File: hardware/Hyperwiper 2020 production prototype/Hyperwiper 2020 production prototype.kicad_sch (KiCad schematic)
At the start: 29 parts, among them J1 Conn_01x05, K1 Main Power relay, K2 Wiper control relay, Q1 PN2222A, Q2 IRF540N, SW1 ON-OFF, SW2 SW_Reed, U1 Teensy4.0, U3 Voltage regulator

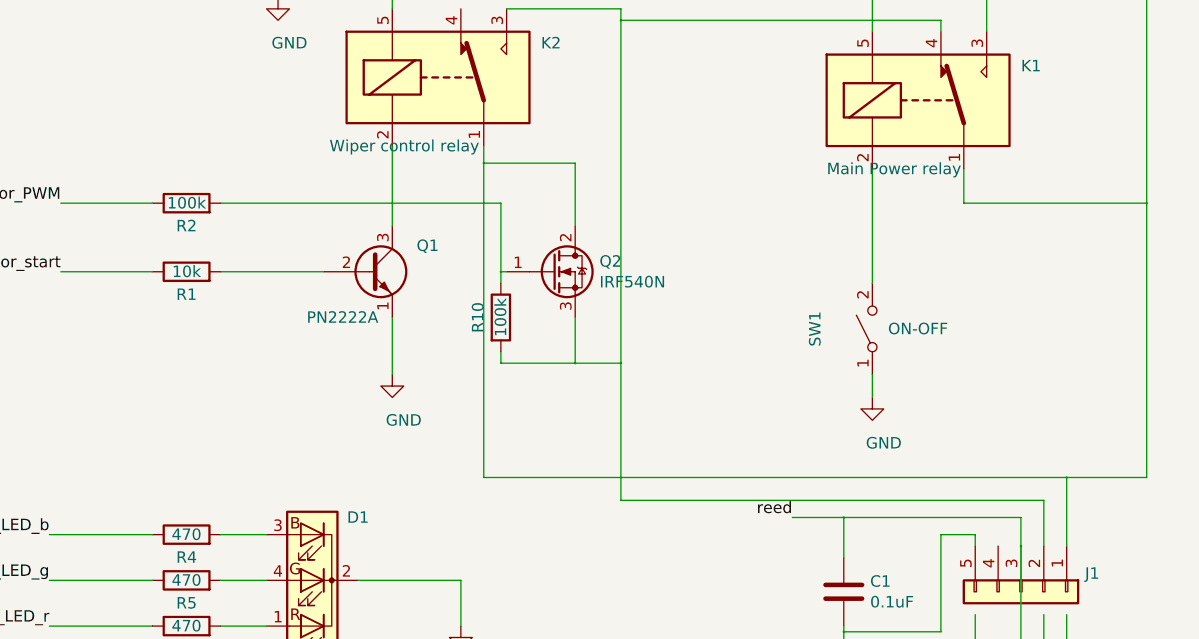
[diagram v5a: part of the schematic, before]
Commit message: Updated board for  level chnages MOSFET.
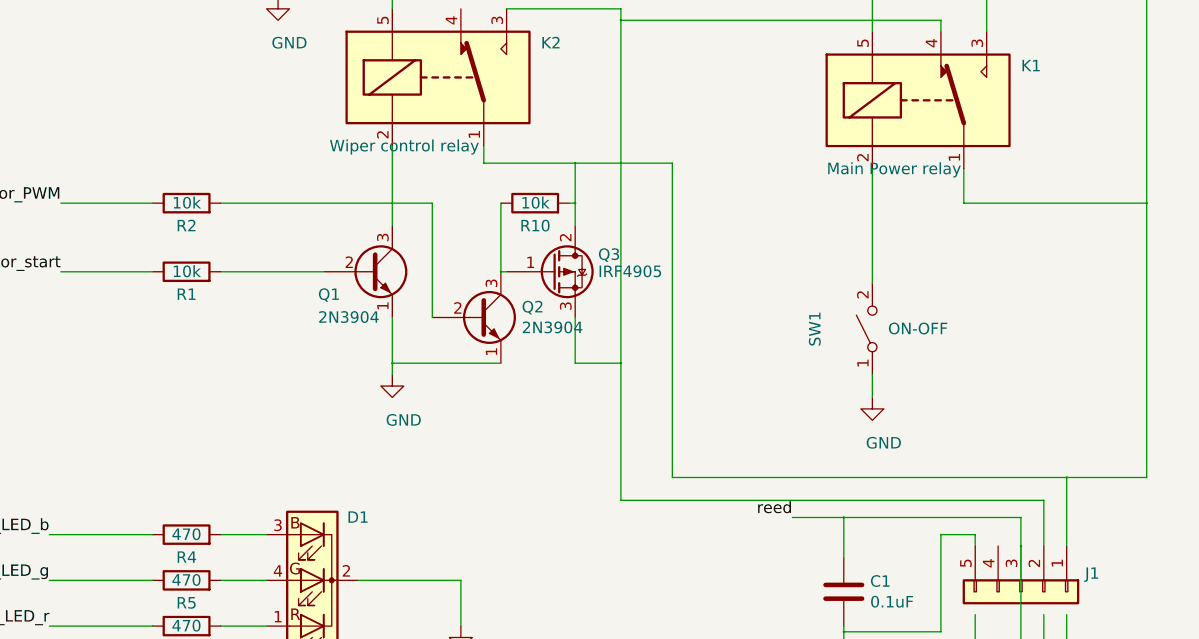
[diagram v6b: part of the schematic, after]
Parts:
- added Q2: 2N3904, Package_TO_SOT_THT:TO-92_Inline, symbol Transistor_BJT:2N3904
- Q1: value PN2222A -> 2N3904; symbol Transistor_BJT:PN2222A -> Transistor_BJT:2N3904
- Q3: renamed from Q2; value IRF540N -> IRF4905; symbol Transistor_FET:IRF540N -> Transistor_FET:IRF4905
- R10, R2: value 100k -> 10k
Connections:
- net GND: now also Q2.1 (E)
- net at Q3.1 (G), R10.1: now also Q2.3 (C); no longer R2.2
- net at J1.1 (Pin_1), K1.1, K1.5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: now also R10.2
- net at J1.2 (Pin_2), K1.4, K2.3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: no longer R10.2
- new net: Q2.2 (B), R2.2
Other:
- moved on the sheet: R10
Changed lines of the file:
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@@
   )
   (junction (at 179.07 20.32) (diameter 0.259) (color 0 0 0 0))
-  (junction (at 201.93 70.485) (diameter 0.259) (color 0 0 0 0))
+  (junction (at 191.77 92.71) (diameter 0.259) (color 0 0 0 0))
   (junction (at 203.835 82.55) (diameter 0.259) (color 0 0 0 0))
   (junction (at 207.645 33.02) (diameter 0.259) (color 0 0 0 0))
-  (junction (at 212.09 92.71) (diameter 0.259) (color 0 0 0 0))
+  (junction (at 212.09 70.485) (diameter 0.259) (color 0 0 0 0))
+  (junction (at 212.09 74.93) (diameter 0.259) (color 0 0 0 0))
   (junction (at 213.36 20.32) (diameter 0.259) (color 0 0 0 0))
   (junction (at 217.17 54.61) (diameter 0.259) (color 0 0 0 0))
@@
     (stroke (width 0) (type solid) (color 0 0 0 0))
   )
-  (wire (pts (xy 172.72 74.93) (xy 203.835 74.93))
-    (stroke (width 0) (type solid) (color 0 0 0 0))
-  )
   (wire (pts (xy 172.72 82.55) (xy 184.15 82.55))
     (stroke (width 0) (type solid) (color 0 0 0 0))
@@
     (stroke (width 0) (type solid) (color 0 0 0 0))
   )
-  (wire (pts (xy 191.77 87.63) (xy 191.77 93.98))
+  (wire (pts (xy 191.77 87.63) (xy 191.77 92.71))
+    (stroke (width 0) (type solid) (color 0 0 0 0))
+  )
+  (wire (pts (xy 191.77 92.71) (xy 191.77 93.98))
+    (stroke (width 0) (type solid) (color 0 0 0 0))
+  )
+  (wire (pts (xy 196.215 74.93) (xy 172.72 74.93))
+    (stroke (width 0) (type solid) (color 0 0 0 0))
+  )
+  (wire (pts (xy 196.215 87.63) (xy 196.215 74.93))
     (stroke (width 0) (type solid) (color 0 0 0 0))
   )
@@
     (stroke (width 0) (type solid) (color 0 0 0 0))
   )
-  (wire (pts (xy 201.93 70.485) (xy 201.93 105.41))
-    (stroke (width 0) (type solid) (color 0 0 0 0))
-  )
   (wire (pts (xy 201.93 70.485) (xy 212.09 70.485))
     (stroke (width 0) (type solid) (color 0 0 0 0))
   )
-  (wire (pts (xy 201.93 105.41) (xy 266.7 105.41))
-    (stroke (width 0) (type solid) (color 0 0 0 0))
-  )
   (wire (pts (xy 203.2 33.02) (xy 207.645 33.02))
     (stroke (width 0) (type solid) (color 0 0 0 0))
@@
     (stroke (width 0) (type solid) (color 0 0 0 0))
   )
-  (wire (pts (xy 203.835 83.82) (xy 203.835 82.55))
-    (stroke (width 0) (type solid) (color 0 0 0 0))
-  )
-  (wire (pts (xy 203.835 92.71) (xy 203.835 91.44))
-    (stroke (width 0) (type solid) (color 0 0 0 0))
-  )
-  (wire (pts (xy 203.835 92.71) (xy 212.09 92.71))
+  (wire (pts (xy 203.835 92.71) (xy 191.77 92.71))
     (stroke (width 0) (type solid) (color 0 0 0 0))
   )
@@
     (stroke (width 0) (type solid) (color 0 0 0 0))
   )
-  (wire (pts (xy 212.09 70.485) (xy 212.09 77.47))
+  (wire (pts (xy 211.455 74.93) (xy 212.09 74.93))
+    (stroke (width 0) (type solid) (color 0 0 0 0))
+  )
+  (wire (pts (xy 212.09 70.485) (xy 212.09 74.93))
+    (stroke (width 0) (type solid) (color 0 0 0 0))
+  )
+  (wire (pts (xy 212.09 74.93) (xy 212.09 77.47))
     (stroke (width 0) (type solid) (color 0 0 0 0))
   )
@@
   )
   (wire (pts (xy 217.17 107.95) (xy 264.16 107.95))
+    (stroke (width 0) (type solid) (color 0 0 0 0))
+  )
+  (wire (pts (xy 222.885 70.485) (xy 212.09 70.485))
+    (stroke (width 0) (type solid) (color 0 0 0 0))
+  )
+  (wire (pts (xy 222.885 70.485) (xy 222.885 105.41))
+    (stroke (width 0) (type solid) (color 0 0 0 0))
+  )
+  (wire (pts (xy 222.885 105.41) (xy 266.7 105.41))
     (stroke (width 0) (type solid) (color 0 0 0 0))
   )
@@
     (in_bom yes) (on_board yes)
     (property "Reference" "R2" (id 0) (at 168.91 77.47 90))
-    (property "Value" "100k" (id 1) (at 168.91 74.93 90))
+    (property "Value" "10k" (id 1) (at 168.91 74.93 90))
     (property "Footprint" "Resistor_THT:R_Axial_DIN0207_L6.3mm_D2.5mm_P10.16mm_Horizontal" (id 2) (at 168.91 76.708 90)
       (effects (font (size 1.27 1.27)) hide)
@@
     (pin "2")
   )
-  (symbol (lib_id "Device:R") (at 203.835 87.63 0) (unit 1)
-    (in_bom yes) (on_board yes)
-    (property "Reference" "R10" (id 0) (at 201.295 87.63 90))
-    (property "Value" "100k" (id 1) (at 203.835 87.63 90))
-    (property "Footprint" "Resistor_THT:R_Axial_DIN0207_L6.3mm_D2.5mm_P10.16mm_Horizontal" (id 2) (at 202.057 87.63 90)
-      (effects (font (size 1.27 1.27)) hide)
-    )
-    (property "Datasheet" "~" (id 3) (at 203.835 87.63 0)
+  (symbol (lib_id "Device:R") (at 207.645 74.93 90) (unit 1)
+    (in_bom yes) (on_board yes)
+    (property "Reference" "R10" (id 0) (at 207.645 77.47 90))
+    (property "Value" "10k" (id 1) (at 207.645 74.93 90))
+    (property "Footprint" "Resistor_THT:R_Axial_DIN0207_L6.3mm_D2.5mm_P10.16mm_Horizontal" (id 2) (at 207.645 76.708 90)
+      (effects (font (size 1.27 1.27)) hide)
+    )
+    (property "Datasheet" "~" (id 3) (at 207.645 74.93 0)
       (effects (font (size 1.27 1.27)) hide)
     )
@@
     (pin "5")
   )
-  (symbol (lib_id "Transistor_BJT:PN2222A") (at 189.23 82.55 0) (unit 1)
-    (in_bom yes) (on_board yes)
-    (property "Reference" "Q1" (id 0) (at 194.4624 79.6544 0)
-      (effects (font (size 1.27 1.27)) (justify left))
-    )
-    (property "Value" "PN2222A" (id 1) (at 182.245 87.63 0)
+  (symbol (lib_id "Transistor_BJT:2N3904") (at 189.23 82.55 0) (unit 1)
+    (in_bom yes) (on_board yes)
+    (property "Reference" "Q1" (id 0) (at 183.515 85.09 0)
+      (effects (font (size 1.27 1.27)) (justify left))
+    )
+    (property "Value" "2N3904" (id 1) (at 183.515 87.63 0)
       (effects (font (size 1.27 1.27)) (justify left))
     )
@@
       (effects (font (size 1.27 1.27) italic) (justify left) hide)
     )
-    (property "Datasheet" "http://www.fairchildsemi.com/ds/PN/PN2222A.pdf" (id 3) (at 189.23 82.55 0)
+    (property "Datasheet" "https://www.fairchildsemi.com/datasheets/2N/2N3904.pdf" (id 3) (at 189.23 82.55 0)
       (effects (font (size 1.27 1.27)) (justify left) hide)
     )
@@
     (pin "3")
   )
-  (symbol (lib_id "Transistor_FET:IRF540N") (at 209.55 82.55 0) (unit 1)
-    (in_bom yes) (on_board yes)
-    (property "Reference" "Q2" (id 0) (at 214.7825 81.4006 0)
-      (effects (font (size 1.27 1.27)) (justify left))
-    )
-    (property "Value" "IRF540N" (id 1) (at 214.7825 83.6993 0)
-      (effects (font (size 1.27 1.27)) (justify left))
-    )
-    (property "Footprint" "Package_TO_SOT_THT:TO-220-3_Vertical" (id 2) (at 215.9 84.455 0)
+  (symbol (lib_id "Transistor_BJT:2N3904") (at 201.295 87.63 0) (unit 1)
+    (in_bom yes) (on_board yes)
+    (property "Reference" "Q2" (id 0) (at 206.1465 86.4806 0)
+      (effects (font (size 1.27 1.27)) (justify left))
+    )
+    (property "Value" "2N3904" (id 1) (at 206.1465 88.7793 0)
+      (effects (font (size 1.27 1.27)) (justify left))
+    )
+    (property "Footprint" "Package_TO_SOT_THT:TO-92_Inline" (id 2) (at 206.375 89.535 0)
       (effects (font (size 1.27 1.27) italic) (justify left) hide)
     )
-    (property "Datasheet" "http://www.irf.com/product-info/datasheets/data/irf540n.pdf" (id 3) (at 209.55 82.55 0)
+    (property "Datasheet" "https://www.fairchildsemi.com/datasheets/2N/2N3904.pdf" (id 3) (at 201.295 87.63 0)
+      (effects (font (size 1.27 1.27)) (justify left) hide)
+    )
+    (pin "1")
+    (pin "2")
+    (pin "3")
+  )
+  (symbol (lib_id "Transistor_FET:IRF4905") (at 209.55 82.55 0) (unit 1)
+    (in_bom yes) (on_board yes)
+    (property "Reference" "Q3" (id 0) (at 214.63 80.645 0)
+      (effects (font (size 1.27 1.27)) (justify left))
+    )
+    (property "Value" "IRF4905" (id 1) (at 214.63 82.55 0)
+      (effects (font (size 1.27 1.27)) (justify left))
+    )
+    (property "Footprint" "Package_TO_SOT_THT:TO-220-3_Vertical" (id 2) (at 214.63 84.455 0)
+      (effects (font (size 1.27 1.27) italic) (justify left) hide)
+    )
+    (property "Datasheet" "http://www.infineon.com/dgdl/irf4905.pdf?fileId=5546d462533600a4015355e32165197c" (id 3) (at 209.55 82.55 0)
       (effects (font (size 1.27 1.27)) (justify left) hide)
     )
@@
     )
     (path "/33d73d81-9a59-421e-853e-603a76a5a74f"
-      (reference "Q1") (unit 1) (value "PN2222A") (footprint "Package_TO_SOT_THT:TO-92_Inline")
+      (reference "Q1") (unit 1) (value "2N3904") (footprint "Package_TO_SOT_THT:TO-92_Inline")
+    )
+    (path "/6318e5ba-d851-4b22-a87c-1d3af44d9c31"
+      (reference "Q2") (unit 1) (value "2N3904") (footprint "Package_TO_SOT_THT:TO-92_Inline")
     )
     (path "/42ff64b0-da36-4f71-aae5-936b46e4405a"
-      (reference "Q2") (unit 1) (value "IRF540N") (footprint "Package_TO_SOT_THT:TO-220-3_Vertical")
+      (reference "Q3") (unit 1) (value "IRF4905") (footprint "Package_TO_SOT_THT:TO-220-3_Vertical")
     )
     (path "/65686585-9a82-487b-a854-2009679eaabf"
@@
     )
     (path "/1fcecf2b-4e2f-4005-a609-f08496f7cf92"
-      (reference "R2") (unit 1) (value "100k") (footprint "Resistor_THT:R_Axial_DIN0207_L6.3mm_D2.5mm_P10.16mm_Horizontal")
+      (reference "R2") (unit 1) (value "10k") (footprint "Resistor_THT:R_Axial_DIN0207_L6.3mm_D2.5mm_P10.16mm_Horizontal")
     )
     (path "/76aee86c-aa88-408e-8da8-0d615fb3331c"
@@
     )
     (path "/262574bc-5200-41bf-819f-e4ebc4aa93eb"
-      (reference "R10") (unit 1) (value "100k") (footprint "Resistor_THT:R_Axial_DIN0207_L6.3mm_D2.5mm_P10.16mm_Horizontal")
+      (reference "R10") (unit 1) (value "10k") (footprint "Resistor_THT:R_Axial_DIN0207_L6.3mm_D2.5mm_P10.16mm_Horizontal")
     )
     (path "/3c75595d-bef3-4439-a823-4b03a4737025"

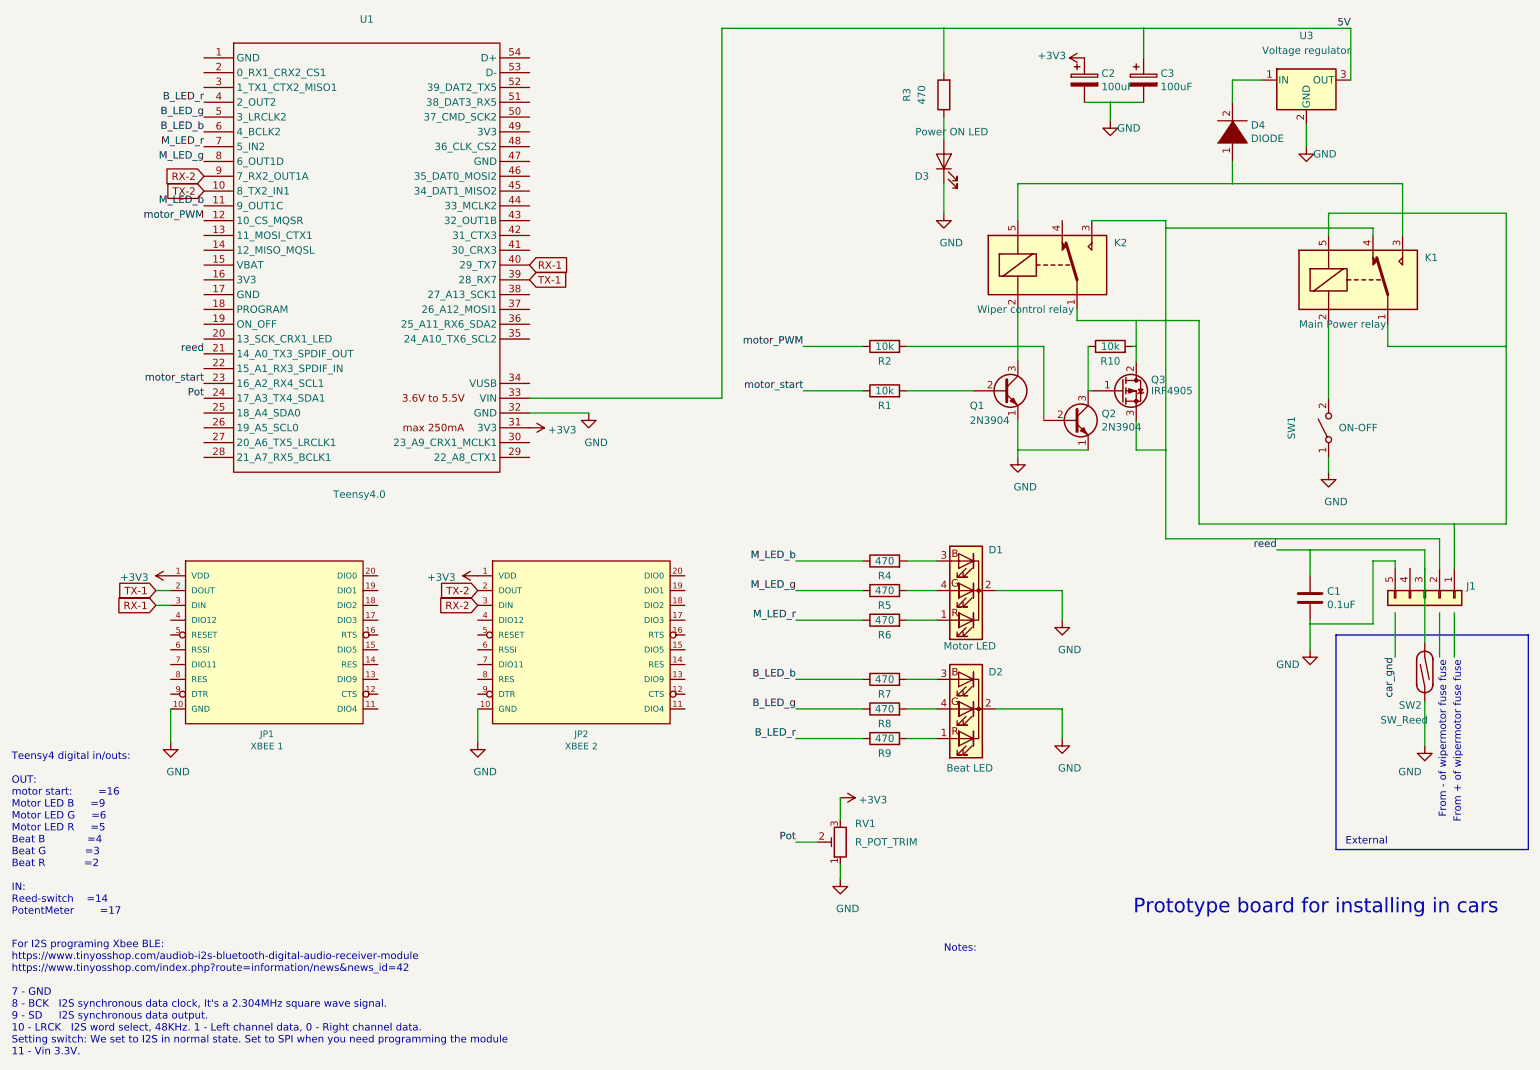
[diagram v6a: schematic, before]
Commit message: Updated schematic to V2.1.6 (MOSFETS)
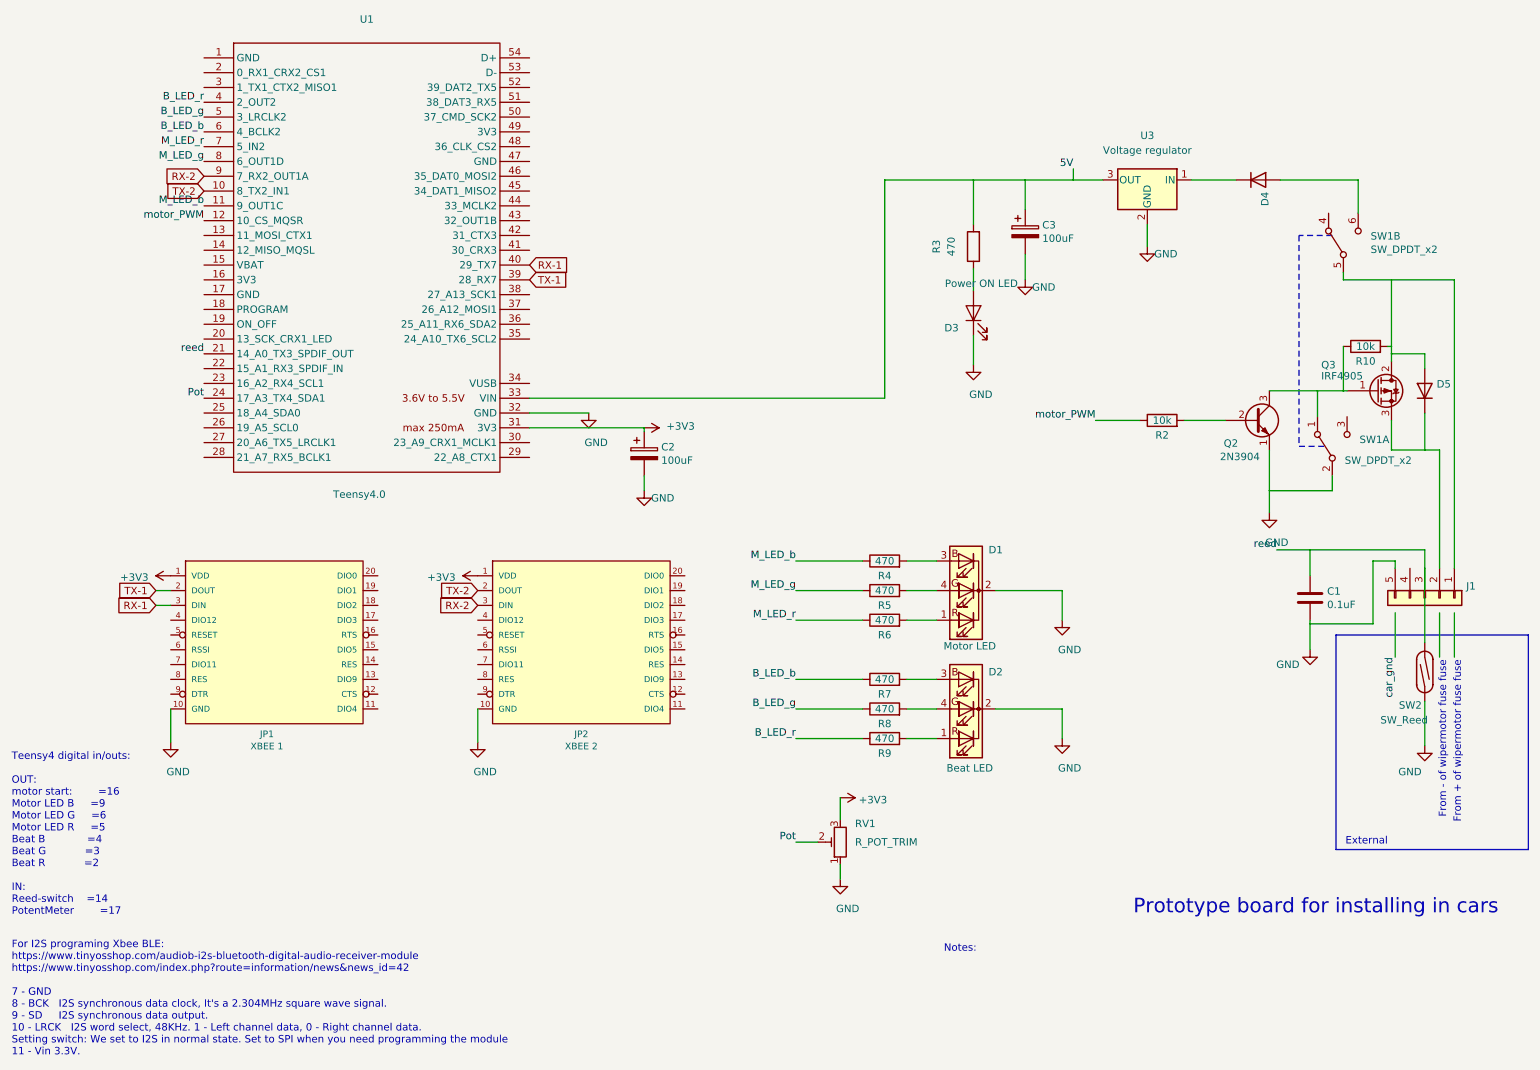
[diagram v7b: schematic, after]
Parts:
- removed D4: DIODE, Diode_THT:D_DO-15_P15.24mm_Horizontal, symbol pspice:DIODE
- removed K1: Main Power relay, Relay_THT:Relay_SPDT_SANYOU_SRD_Series_Form_C, symbol Relay:SANYOU_SRD_Form_C
- removed K2: Wiper control relay, Relay_THT:Relay_SPDT_SANYOU_SRD_Series_Form_C, symbol Relay:SANYOU_SRD_Form_C
- removed Q1: 2N3904, Package_TO_SOT_THT:TO-92_Inline, symbol Transistor_BJT:2N3904
- removed R1: 10k, Resistor_THT:R_Axial_DIN0207_L6.3mm_D2.5mm_P10.16mm_Horizontal, symbol Device:R
- removed SW1: ON-OFF, Button_Switch_THT:SW_Tactile_SPST_Angled_PTS645Vx83-2LFS, symbol Switch:SW_SPST
- added D4, D5: DIODE, symbol Simulation_SPICE:DIODE
- added SW1: SW_DPDT_x2, symbol Switch:SW_DPDT_x2
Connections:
- net GND: now also SW1.2 (B)
- net at J1.1 (Pin_1), Q3.2 (D), R10.2: now also D5.1 (A), SW1.5 (B)
- net at J1.2 (Pin_2), Q3.3 (S): now also D5.2 (K)
- net at Q2.3 (C), Q3.1 (G), R10.1: now also SW1.1 (A)
- net at U3.1 (IN): now also D4.2 (K)
- net motor_start: no longer names the net of U1.23 (16_A2_RX4_SCL1)
- new net: D4.1 (A), SW1.6 (C)
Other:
- moved on the sheet: C2, C3, D3, Q2, Q3, R10, R2, R3, U3
